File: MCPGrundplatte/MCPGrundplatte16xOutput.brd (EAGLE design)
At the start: 79.7 x 80 mm, 8 parts, among them IC1 ULN2803, IC4 ULN2803, X1GPA0-7 MKDSN1,5/9-5,08, X2 MKDSN1,5/2-5,08, X2GPB0-7 MKDSN1,5/9-5,08

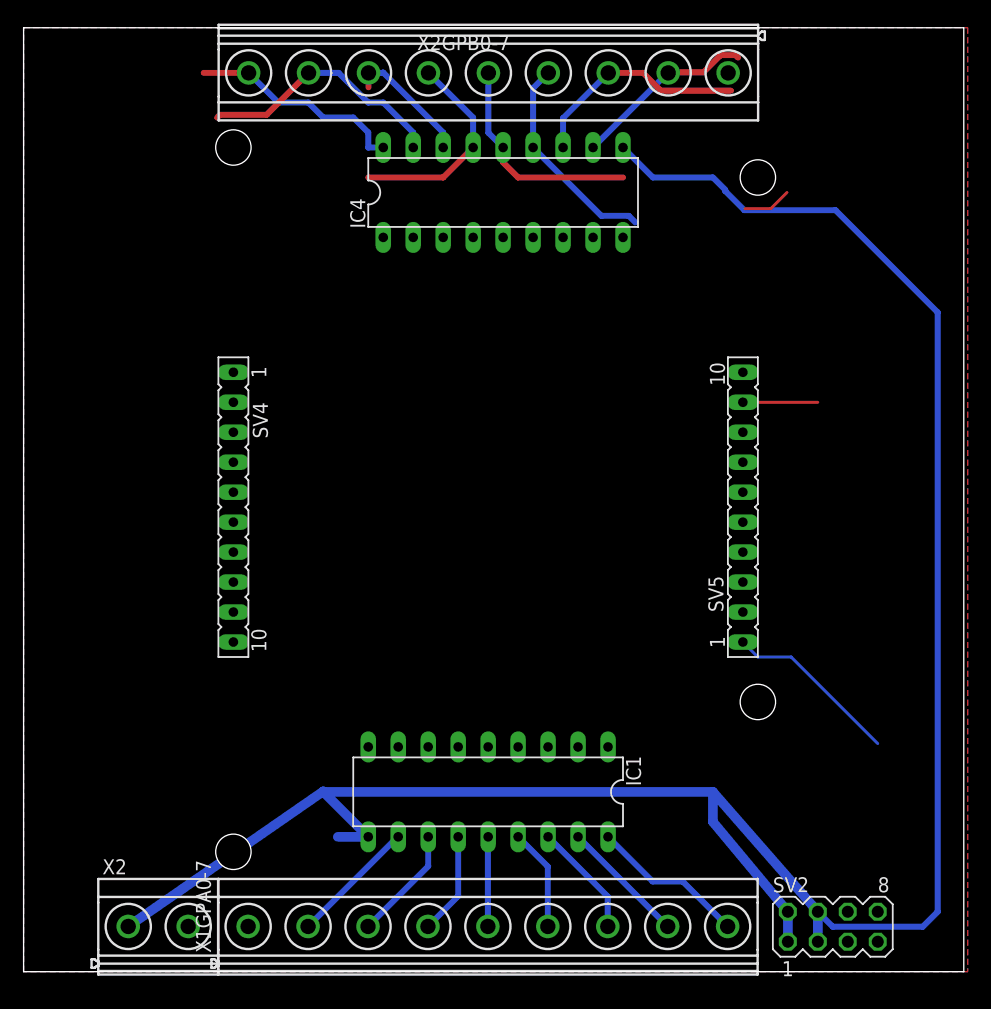
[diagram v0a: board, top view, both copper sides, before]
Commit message: Neuen OutPut 16x hinzugefügt
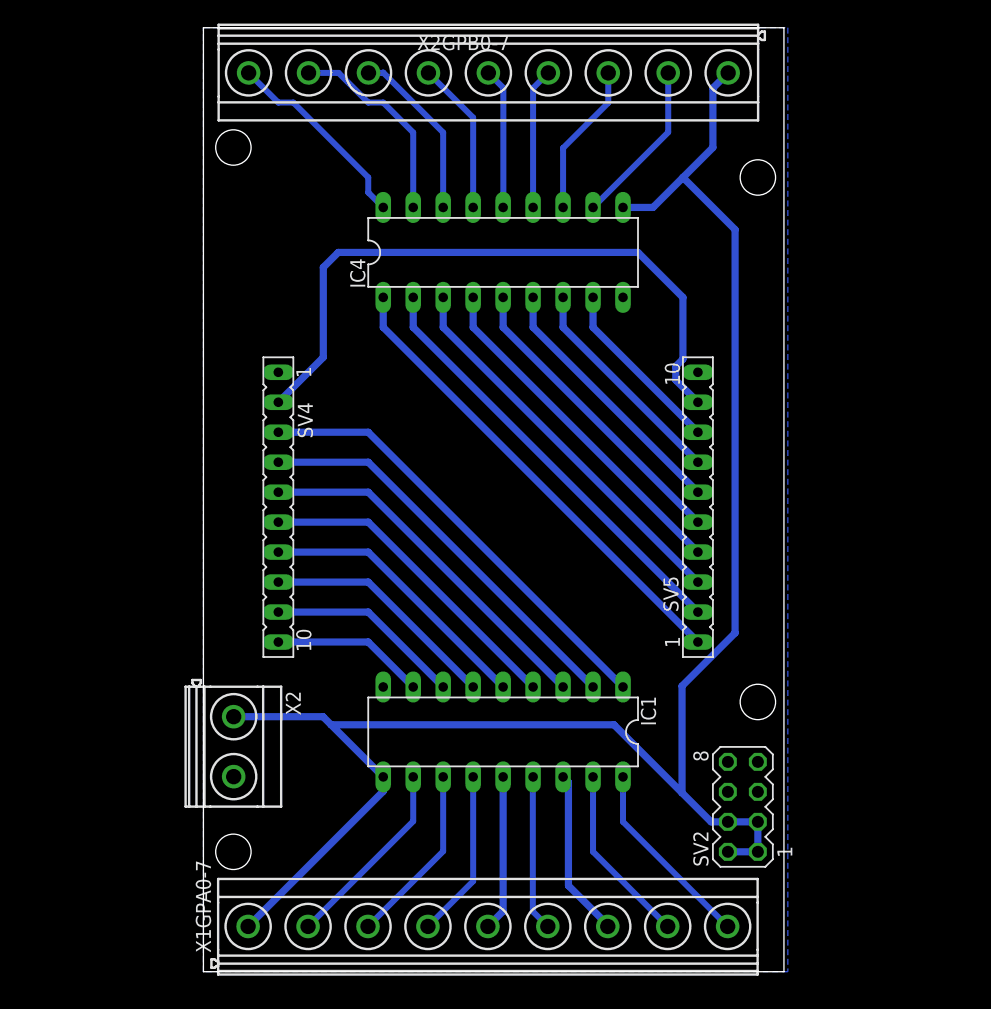
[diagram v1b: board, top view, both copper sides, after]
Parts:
- moved X2 16.5 mm to (2.54, 19.1), turned to 270 degrees
- moved SV2 12.7 mm to (45.7, 14.0), turned to 90 degrees
- moved IC1 5.24 mm to (25.4, 20.3)
- moved IC4 5.08 mm to (25.4, 61.0)
- moved SV5 3.81 mm to (41.9, 39.4)
- moved SV4 3.81 mm to (6.35, 39.4)
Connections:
- net +12V: now also X2GPB0-7.1
- net GND: no longer X2GPB0-7.1
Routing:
- net VDD: track 6.35 -> 55.5 mm
- net N$2: track 0.00 -> 38.2 mm
- net +12V: track 186.7 -> 149.3 mm
- net GPB1.: track 0.00 -> 36.7 mm
- net N$3: track 0.00 -> 34.6 mm
- net GPB2.: track 0.00 -> 33.1 mm
- net N$4: track 0.00 -> 31.0 mm
- net GPB3.: track 0.00 -> 29.5 mm
- net N$5: track 0.00 -> 27.4 mm
- net GPB4.: track 0.00 -> 25.9 mm
- net GPB0.: track 15.0 -> 40.3 mm
- net N$6: track 0.00 -> 23.8 mm
- net GPB5.: track 0.00 -> 22.3 mm
- net N$1: track 0.00 -> 20.2 mm
- net GPB6.: track 0.00 -> 18.7 mm
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- removed copper zone on layer 1, net GND
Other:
- board size 79.7 x 80 mm -> 49.2 x 80 mm
- board text added: "SX2MCP23017 16 x OUTPUT Version V1"
- board text removed: "SX2MCP23017 INPUT Version V5"

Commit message: Aktuallisiert
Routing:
- net GPB1: track 17.3 -> 15.8 mm
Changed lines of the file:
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@@
 <contactref element="IC4" pad="17"/>
 <contactref element="X2GPB0-7" pad="8"/>
-<wire x1="8.9111" y1="76.175" x2="11.455" y2="76.175" width="0.508" layer="16"/>
-<wire x1="13.97" y1="73.66" x2="11.455" y2="76.175" width="0.508" layer="16"/>
-<wire x1="17.78" y1="64.77" x2="17.78" y2="71.12" width="0.508" layer="16"/>
-<wire x1="17.78" y1="71.12" x2="15.24" y2="73.66" width="0.508" layer="16"/>
-<wire x1="15.24" y1="73.66" x2="13.97" y2="73.66" width="0.508" layer="16"/>
+<wire x1="8.9111" y1="76.175" x2="10.185" y2="76.175" width="0.508" layer="16"/>
+<wire x1="16.51" y1="69.85" x2="10.185" y2="76.175" width="0.508" layer="16"/>
+<wire x1="17.78" y1="64.77" x2="17.78" y2="67.31" width="0.508" layer="16"/>
+<wire x1="17.78" y1="67.31" x2="16.51" y2="68.58" width="0.508" layer="16"/>
+<wire x1="16.51" y1="69.85" x2="16.51" y2="68.58" width="0.508" layer="16"/>
 </signal>
 <signal name="GPB5">
@@
 <contactref element="IC4" pad="11"/>
 <contactref element="X2GPB0-7" pad="2"/>
-<wire x1="39.3911" y1="76.175" x2="39.3911" y2="71.1411" width="0.508" layer="16"/>
-<wire x1="39.3911" y1="71.1411" x2="33.02" y2="64.77" width="0.508" layer="16"/>
-<wire x1="39.3911" y1="76.2211" x2="39.3911" y2="76.175" width="0.254" layer="1"/>
+<wire x1="39.3911" y1="76.175" x2="39.3911" y2="73.6811" width="0.6096" layer="16"/>
+<wire x1="33.02" y1="64.77" x2="33.02" y2="67.31" width="0.6096" layer="16"/>
+<wire x1="39.3911" y1="73.6811" x2="33.02" y2="67.31" width="0.6096" layer="16"/>
 </signal>
 <signal name="GPB7.">

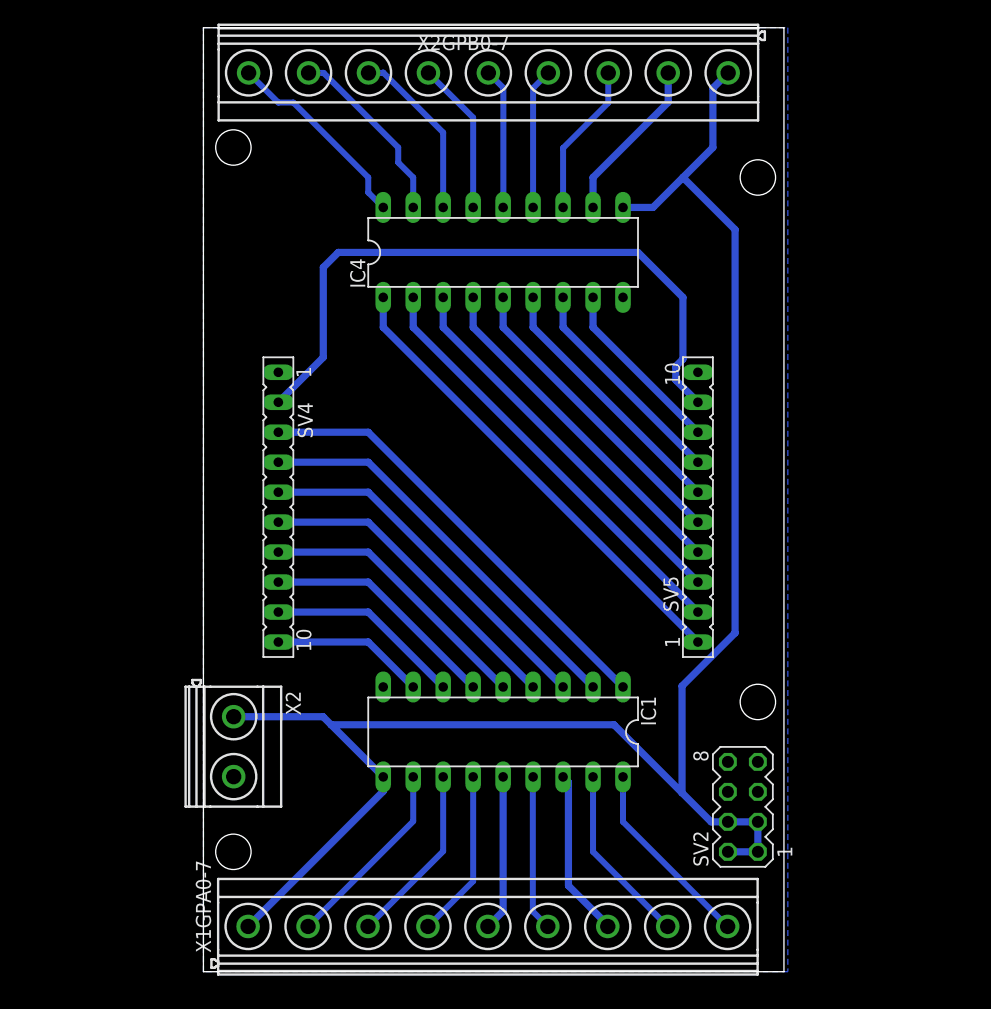
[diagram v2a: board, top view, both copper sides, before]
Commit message: Siebdruck angepasst, C hinzugefügt
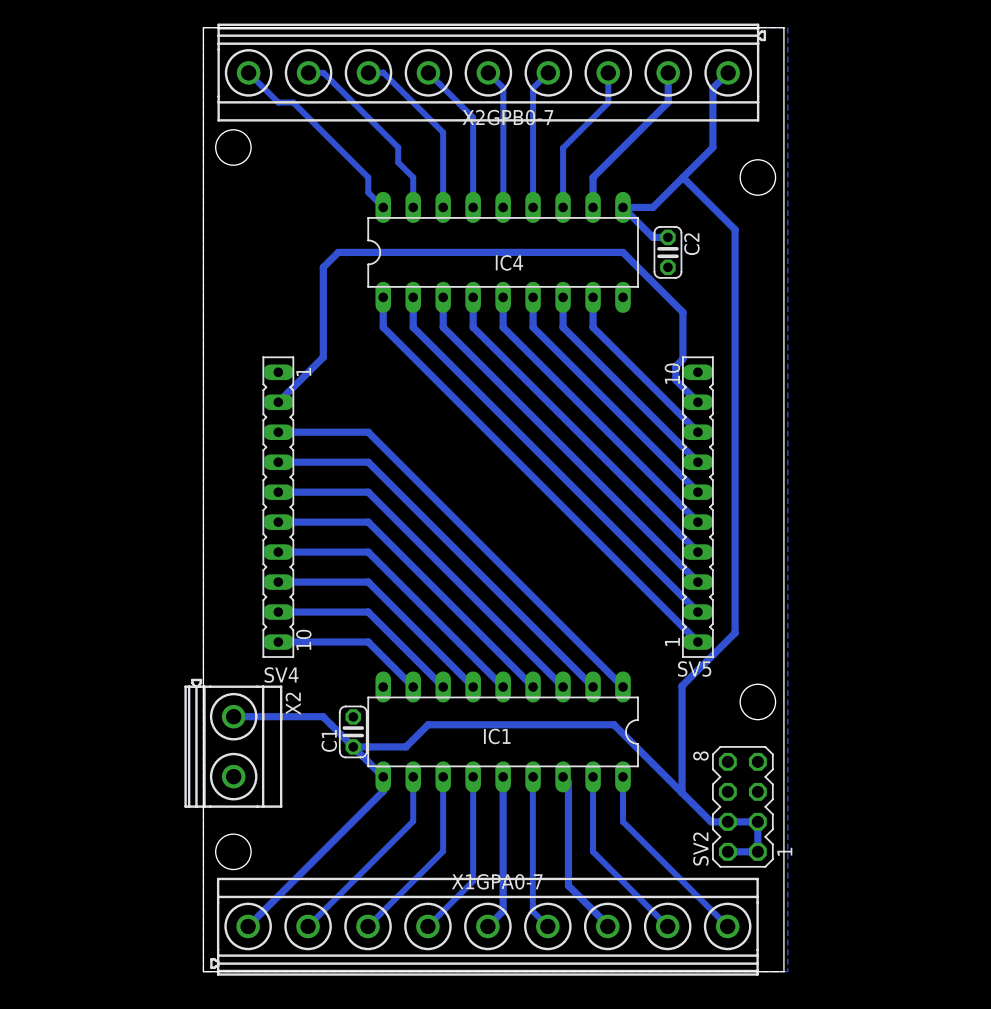
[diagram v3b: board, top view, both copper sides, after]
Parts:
- added C1, C2: (no value), rcl:C025-024X044
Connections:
- net +12V: now also C1.1, C2.1
- net GND: now also C1.2, C2.2
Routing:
- net +12V: track 149.3 -> 153.1 mm
- net VDD: track 55.5 -> 54.8 mm
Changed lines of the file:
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@@
 <elements>
 <element name="X1GPA0-7" library="con-phoenix-508" library_urn="urn:adsk.eagle:library:176" package="MKDSN1,5/9-5,08" package3d_urn="urn:adsk.eagle:package:9637/1" value="MKDSN1,5/9-5,08" x="24.13" y="3.81" smashed="yes">
-<attribute name="NAME" x="0.635" y="1.5989" size="1.27" layer="25" rot="R90"/>
+<attribute name="NAME" x="28.8811" y="8.255" size="1.27" layer="25" rot="R180"/>
 <attribute name="POPULARITY" value="1" x="60.96" y="-26.67" size="1.778" layer="27" display="off"/>
-<attribute name="VALUE" x="17.78" y="5.715" size="1.27" layer="27"/>
 </element>
 <element name="X2GPB0-7" library="con-phoenix-508" library_urn="urn:adsk.eagle:library:176" package="MKDSN1,5/9-5,08" package3d_urn="urn:adsk.eagle:package:9637/1" value="MKDSN1,5/9-5,08" x="24.13" y="76.2" smashed="yes" rot="R180">
-<attribute name="NAME" x="18.1089" y="78.105" size="1.27" layer="25"/>
+<attribute name="NAME" x="21.9189" y="71.755" size="1.27" layer="25"/>
 <attribute name="POPULARITY" value="1" x="-12.7" y="118.11" size="1.778" layer="27" rot="R180" display="off"/>
-<attribute name="VALUE" x="38.1" y="74.295" size="1.27" layer="27" rot="R180"/>
 </element>
 <element name="SV4" library="con-lsta" library_urn="urn:adsk.eagle:library:161" package="FE10" package3d_urn="urn:adsk.eagle:package:8192/1" value="" x="6.35" y="39.37" smashed="yes" rot="R270">
 <attribute name="MF" value="" x="6.35" y="39.37" size="1.778" layer="27" rot="R270" display="off"/>
 <attribute name="MPN" value="" x="6.35" y="39.37" size="1.778" layer="27" rot="R270" display="off"/>
-<attribute name="NAME" x="8.001" y="48.26" size="1.27" layer="25" ratio="10" rot="R270"/>
+<attribute name="NAME" x="5.08" y="24.511" size="1.27" layer="25" ratio="10"/>
 <attribute name="OC_FARNELL" value="unknown" x="6.35" y="39.37" size="1.778" layer="27" rot="R270" display="off"/>
 <attribute name="OC_NEWARK" value="unknown" x="6.35" y="39.37" size="1.778" layer="27" rot="R270" display="off"/>
@@
 <attribute name="MF" value="" x="41.91" y="39.37" size="1.778" layer="27" rot="R90" display="off"/>
 <attribute name="MPN" value="" x="41.91" y="39.37" size="1.778" layer="27" rot="R90" display="off"/>
-<attribute name="NAME" x="40.259" y="30.48" size="1.27" layer="25" ratio="10" rot="R90"/>
+<attribute name="NAME" x="43.18" y="26.289" size="1.27" layer="25" ratio="10" rot="R180"/>
 <attribute name="OC_FARNELL" value="unknown" x="41.91" y="39.37" size="1.778" layer="27" rot="R90" display="off"/>
 <attribute name="OC_NEWARK" value="unknown" x="41.91" y="39.37" size="1.778" layer="27" rot="R90" display="off"/>
@@
 </element>
 <element name="IC1" library="uln-udn" library_urn="urn:adsk.eagle:library:407" package="DIL18" package3d_urn="urn:adsk.eagle:package:30237/1" value="ULN2803" x="25.4" y="20.32" smashed="yes" rot="R180">
-<attribute name="NAME" x="37.084" y="23.368" size="1.27" layer="25" ratio="10" rot="R270"/>
-<attribute name="VALUE" x="34.925" y="20.955" size="1.27" layer="27" ratio="10" rot="R180"/>
+<attribute name="NAME" x="23.622" y="19.304" size="1.27" layer="25" ratio="10"/>
 </element>
 <element name="X2" library="con-phoenix-508" library_urn="urn:adsk.eagle:library:176" package="MKDSN1,5/2-5,08" package3d_urn="urn:adsk.eagle:package:9630/1" value="MKDSN1,5/2-5,08" x="2.54" y="19.05" smashed="yes" rot="R270">
 <attribute name="NAME" x="6.985" y="23.8011" size="1.27" layer="25" rot="R270"/>
 <attribute name="POPULARITY" value="14" x="2.54" y="19.05" size="1.778" layer="27" rot="R270" display="off"/>
-<attribute name="VALUE" x="-1.27" y="12.065" size="1.27" layer="27"/>
 </element>
 <element name="SV2" library="con-lstb" library_urn="urn:adsk.eagle:library:162" package="MA04-2" package3d_urn="urn:adsk.eagle:package:8368/1" value="" x="45.72" y="13.97" smashed="yes" rot="R90">
@@
 </element>
 <element name="IC4" library="uln-udn" library_urn="urn:adsk.eagle:library:407" package="DIL18" package3d_urn="urn:adsk.eagle:package:30237/1" value="ULN2803" x="25.4" y="60.96" smashed="yes">
-<attribute name="NAME" x="13.716" y="57.912" size="1.27" layer="25" ratio="10" rot="R90"/>
-<attribute name="VALUE" x="15.875" y="60.325" size="1.27" layer="27" ratio="10"/>
+<attribute name="NAME" x="27.178" y="60.706" size="1.27" layer="25" ratio="10" rot="R180"/>
+</element>
+<element name="C1" library="rcl" library_urn="urn:adsk.eagle:library:334" package="C025-024X044" package3d_urn="urn:adsk.eagle:package:23630/1" value="" x="12.7" y="20.32" smashed="yes" rot="R90">
+<attribute name="NAME" x="11.303" y="18.542" size="1.27" layer="25" ratio="10" rot="R90"/>
+<attribute name="POPULARITY" value="56" x="12.7" y="20.32" size="1.778" layer="27" rot="R90" display="off"/>
+<attribute name="SPICEPREFIX" value="C" x="12.7" y="20.32" size="1.778" layer="27" rot="R90" display="off"/>
+<attribute name="VALUE" x="15.367" y="18.542" size="1.27" layer="27" ratio="10" rot="R90"/>
+</element>
+<element name="C2" library="rcl" library_urn="urn:adsk.eagle:library:334" package="C025-024X044" package3d_urn="urn:adsk.eagle:package:23630/1" value="" x="39.37" y="60.96" smashed="yes" rot="R270">
+<attribute name="NAME" x="40.767" y="62.738" size="1.27" layer="25" ratio="10" rot="R270"/>
+<attribute name="POPULARITY" value="56" x="39.37" y="60.96" size="1.778" layer="27" rot="R270" display="off"/>
+<attribute name="SPICEPREFIX" value="C" x="39.37" y="60.96" size="1.778" layer="27" rot="R270" display="off"/>
+<attribute name="VALUE" x="36.703" y="62.738" size="1.27" layer="27" ratio="10" rot="R270"/>
 </element>
 </elements>
@@
 <wire x1="10.16" y1="52.07" x2="10.16" y2="59.69" width="0.6096" layer="16"/>
 <wire x1="10.16" y1="59.69" x2="11.43" y2="60.96" width="0.6096" layer="16"/>
-<wire x1="11.43" y1="60.96" x2="36.83" y2="60.96" width="0.6096" layer="16"/>
-<wire x1="36.83" y1="60.96" x2="40.64" y2="57.15" width="0.6096" layer="16"/>
+<wire x1="11.43" y1="60.96" x2="35.56" y2="60.96" width="0.6096" layer="16"/>
 <wire x1="40.64" y1="51.9146125" x2="40.0304" y2="51.3050125" width="0.6096" layer="16"/>
 <wire x1="40.0304" y1="51.3050125" x2="40.0304" y2="50.1396" width="0.6096" layer="16"/>
 <wire x1="40.0304" y1="50.1396" x2="41.91" y2="48.26" width="0.6096" layer="16"/>
-<wire x1="40.64" y1="57.15" x2="40.64" y2="51.9146125" width="0.6096" layer="16"/>
+<wire x1="40.64" y1="55.88" x2="40.64" y2="51.9146125" width="0.6096" layer="16"/>
+<wire x1="35.56" y1="60.96" x2="40.64" y2="55.88" width="0.6096" layer="16"/>
 </signal>
 <signal name="GPB2">
@@
 <vertex x="0" y="0"/>
 </polygon>
+<contactref element="C1" pad="2"/>
+<contactref element="C2" pad="2"/>
 </signal>
 <signal name="GPB0.">
@@
 <wire x1="2.565" y1="21.6111" x2="10.1389" y2="21.6111" width="0.6096" layer="16"/>
 <wire x1="10.1389" y1="21.6111" x2="10.8204" y2="20.9296" width="0.6096" layer="16"/>
-<wire x1="10.8204" y1="20.9296" x2="15.24" y2="16.51" width="0.6096" layer="16"/>
 <wire x1="44.45" y1="12.7" x2="43.0246125" y2="12.7" width="0.6096" layer="16"/>
 <wire x1="43.0246125" y1="12.7" x2="40.56230625" y2="15.16230625" width="0.6096" layer="16"/>
 <wire x1="40.56230625" y1="15.16230625" x2="34.7950125" y2="20.9296" width="0.6096" layer="16"/>
-<wire x1="34.7950125" y1="20.9296" x2="10.8204" y2="20.9296" width="0.6096" layer="16"/>
+<wire x1="34.7950125" y1="20.9296" x2="19.05" y2="20.9296" width="0.6096" layer="16"/>
 <wire x1="46.99" y1="10.16" x2="44.45" y2="10.16" width="0.6096" layer="16"/>
 <wire x1="46.99" y1="10.16" x2="46.99" y2="12.7" width="0.6096" layer="16"/>
@@
 <wire x1="45.0596" y1="62.8904" x2="40.64" y2="67.31" width="0.6096" layer="16"/>
 <wire x1="45.0596" y1="28.7049875" x2="45.0596" y2="62.8904" width="0.6096" layer="16"/>
+<contactref element="C1" pad="1"/>
+<contactref element="C2" pad="1"/>
+<wire x1="39.37" y1="62.23" x2="38.1" y2="62.23" width="0.6096" layer="16"/>
+<wire x1="38.1" y1="62.23" x2="35.56" y2="64.77" width="0.6096" layer="16"/>
+<wire x1="15.24" y1="16.51" x2="12.7" y2="19.05" width="0.6096" layer="16"/>
+<wire x1="12.7" y1="19.05" x2="10.8204" y2="20.9296" width="0.6096" layer="16"/>
+<wire x1="19.05" y1="20.9296" x2="17.1704" y2="19.05" width="0.6096" layer="16"/>
+<wire x1="17.1704" y1="19.05" x2="12.7" y2="19.05" width="0.6096" layer="16"/>
 </signal>
 <signal name="GPA7">
